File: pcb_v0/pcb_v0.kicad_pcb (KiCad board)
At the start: 2 copper layers, 1 part, among them U1 ATtiny2313-20P

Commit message: saved
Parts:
- added J1: Screw_Terminal_01x03, TerminalBlock_MetzConnect:TerminalBlock_MetzConnect_Type055_RT01503HDWU_1x03_P5.00mm_Horizontal, F.Cu at (113.1, 67.3)
- added NIX1: ~, nixie:in-8, F.Cu at (151.1, 81.3)
- added NIX2: ~, nixie:in-8, F.Cu at (171.1, 81.3)
- added NIX3: ~, nixie:in-8, F.Cu at (201.1, 81.3)
- added NIX4: ~, nixie:in-8, F.Cu at (221.1, 81.3)
- added NIX5: ~, nixie:in-8, F.Cu at (251.1, 81.3)
- added NIX6: ~, nixie:in-8, F.Cu at (271.1, 81.3)
- added U10: 74141, Package_DIP:DIP-16_W7.62mm_LongPads, F.Cu at (256.5, 71.1)
- added U2: 74141, Package_DIP:DIP-16_W7.62mm_LongPads, F.Cu at (148.6, 71.1)
- added U3: 74141, Package_DIP:DIP-16_W7.62mm_LongPads, F.Cu at (170.2, 71.1)
- added U4: 74141, Package_DIP:DIP-16_W7.62mm_LongPads, F.Cu at (191.8, 71.1)
- added U5: 74LS377, Package_DIP:DIP-20_W7.62mm_LongPads, F.Cu at (199.4, 100.3)
- added U6: 74141, Package_DIP:DIP-16_W7.62mm_LongPads, F.Cu at (213.3, 71.1)
- added U7: 74141, Package_DIP:DIP-16_W7.62mm_LongPads, F.Cu at (234.9, 71.1)
- added U8: 74LS377, Package_DIP:DIP-20_W7.62mm_LongPads, F.Cu at (149.9, 101.6)
- added U9: 74LS377, Package_DIP:DIP-20_W7.62mm_LongPads, F.Cu at (250.2, 100.3)
- moved U1 63.5 mm to (109.2, 17.8)
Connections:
- U1 pad 10: unconnected-(U1-GND-Pad10) -> GND
- U1 pad 12: unconnected-(U1-PB0-Pad12) -> Net-(U1-PB0)
- U1 pad 13: unconnected-(U1-PB1-Pad13) -> Net-(U1-PB1)
- U1 pad 14: unconnected-(U1-PB2-Pad14) -> Net-(U1-PB2)
- U1 pad 15: unconnected-(U1-PB3-Pad15) -> Net-(U1-PB3)
- U1 pad 16: unconnected-(U1-PB4-Pad16) -> Net-(U1-PB4)
- U1 pad 17: unconnected-(U1-PB5-Pad17) -> Net-(U1-PB5)
- U1 pad 18: unconnected-(U1-PB6-Pad18) -> Net-(U1-PB6)
- U1 pad 19: unconnected-(U1-PB7-Pad19) -> Net-(U1-PB7)
- U1 pad 20: unconnected-(U1-VCC-Pad20) -> +5V
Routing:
- net unconnected-(U1-VCC-Pad20): track 59.6 -> 0.00 mm

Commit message: saved
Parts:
- U1: footprint Package_DIP:DIP-20_W7.62mm -> Package_DIP:DIP-20_W7.62mm_LongPads
- moved J1 103.1 mm to (216.0, 61.0)
- moved U2 95.3 mm to (55.8, 49.5)
- moved NIX1 95.3 mm to (58.3, 59.7)
- moved NIX2 95.3 mm to (78.3, 59.7)
- moved NIX3 95.3 mm to (108.3, 59.7)
- moved NIX4 95.3 mm to (128.3, 59.7)
- moved NIX5 95.3 mm to (158.3, 59.7)
- moved NIX6 95.3 mm to (178.3, 59.7)
- moved U3 95.3 mm to (77.4, 49.5)
- moved U4 95.3 mm to (99.0, 49.5)
- moved U6 95.3 mm to (120.6, 49.5)
- moved U7 95.3 mm to (142.1, 49.5)
- moved U9 95.3 mm to (157.4, 78.8)
- moved U10 95.3 mm to (163.7, 49.5)
- moved U8 94.3 mm to (58.3, 78.8)
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
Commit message: saved
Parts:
- U1, U5, U8, U9: footprint Package_DIP:DIP-20_W7.62mm_LongPads -> Package_DIP:DIP-20_W7.62mm
- U10, U2, U3, U4, U6, U7: footprint Package_DIP:DIP-16_W7.62mm_LongPads -> Package_DIP:DIP-16_W7.62mm
- moved J1 165.8 mm to (50.3, 66.0), turned to 90 degrees
- moved U7 14.7 mm to (152.9, 59.6), turned to 160 degrees
- moved U3 13.1 mm to (88.9, 43.3), turned to 20 degrees
- moved U8 10.7 mm to (68.9, 76.9), turned to 80 degrees
- moved U6 10.6 mm to (130.2, 53.8), turned to 120 degrees
- moved U2 10.2 mm to (65.3, 53.2), turned to 103 degrees
- moved NIX1 6.50 mm to (64.4, 62.1)
- moved NIX2 6.50 mm to (84.4, 62.1)
- moved NIX3 6.50 mm to (114.4, 62.1)
- moved NIX4 6.50 mm to (134.4, 62.1)
- moved NIX5 6.50 mm to (164.4, 62.1)
- moved NIX6 6.50 mm to (184.4, 62.1)
- moved U4 6.12 mm to (103.2, 45.1), turned to 60 degrees
- moved U1 5.24 mm to (98.6, 81.2)
- moved U5 5.02 mm to (127.5, 81.2)
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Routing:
- net Net-(U1-PB3): track 0.00 -> 82.1 mm
- net Net-(U1-PB2): track 0.00 -> 71.8 mm
- net Net-(U1-PB1): track 0.00 -> 60.0 mm
- net Net-(U1-PB0): track 0.00 -> 53.8 mm
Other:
- board outline added: 170 x 50 mm

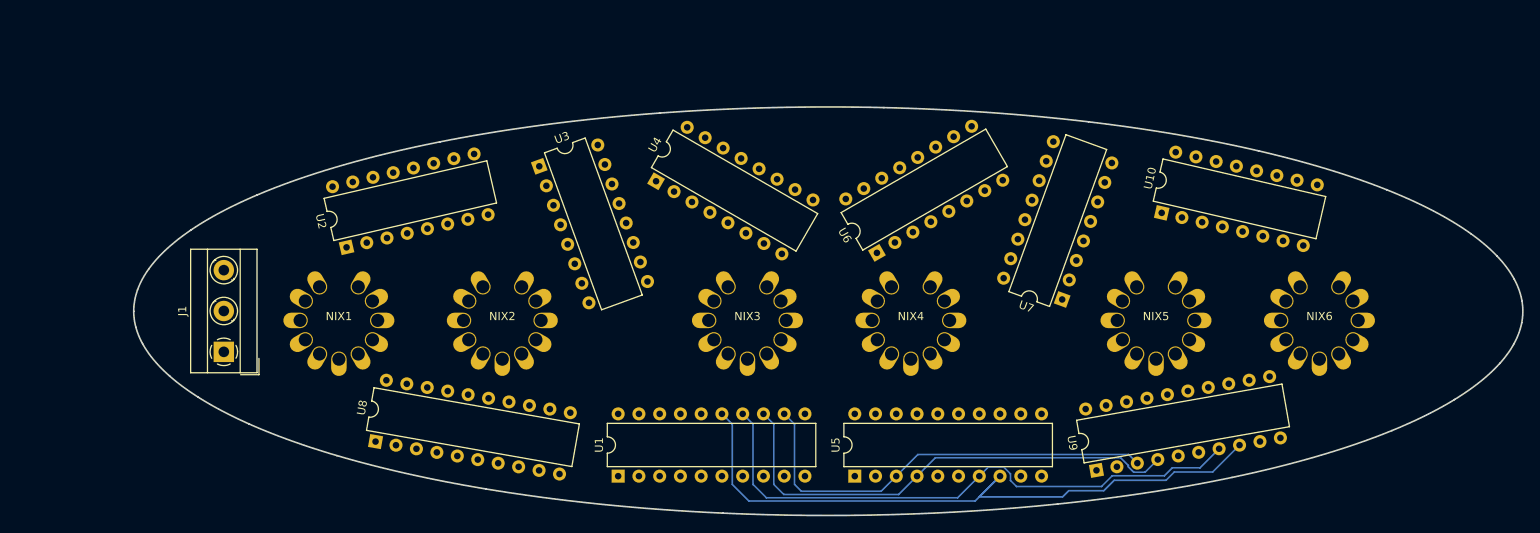
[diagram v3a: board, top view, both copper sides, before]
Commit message: ATtiny and flip flops routed
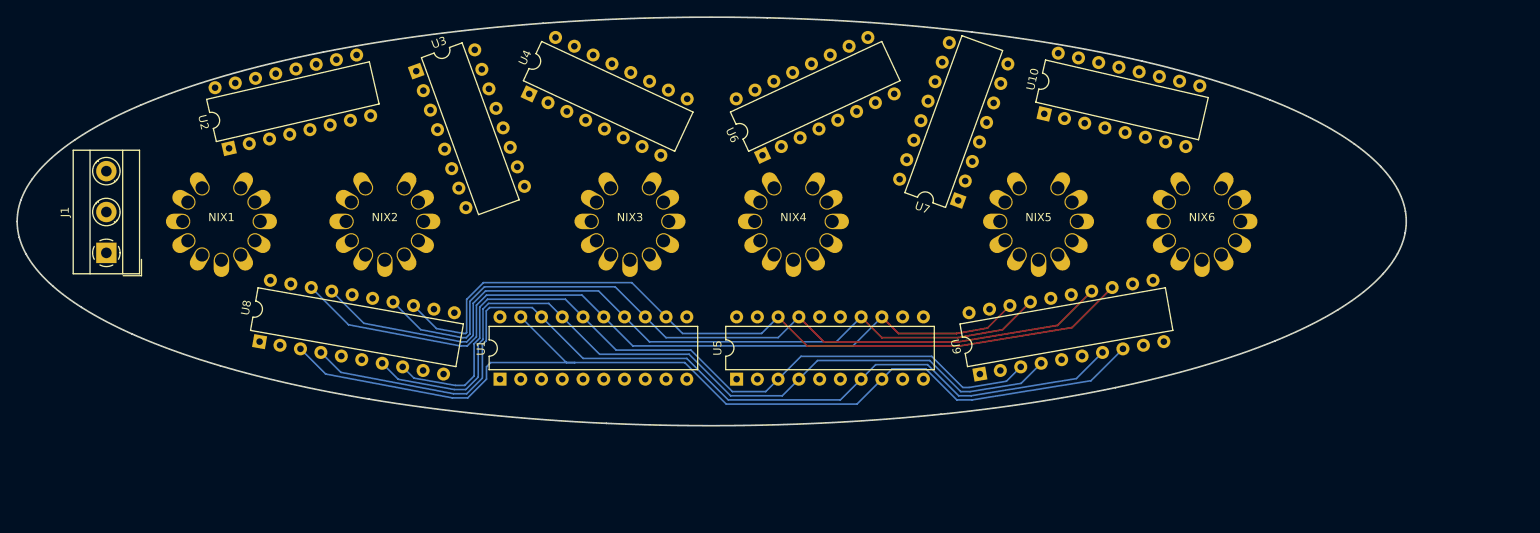
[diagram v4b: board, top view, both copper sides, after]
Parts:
- moved U3 19.0 mm to (73.8, 31.6)
- moved U4 18.8 mm to (87.7, 34.4), turned to 65 degrees
- moved U10 18.8 mm to (150.7, 36.8)
- moved J1 18.8 mm to (35.9, 53.8)
- moved NIX1 18.8 mm to (50.0, 50.0)
- moved NIX2 18.8 mm to (70.0, 50.0)
- moved NIX3 18.8 mm to (100.0, 50.0)
- moved NIX4 18.8 mm to (120.0, 50.0)
- moved NIX5 18.8 mm to (150.0, 50.0)
- moved NIX6 18.8 mm to (170.0, 50.0)
- moved U2 18.8 mm to (50.9, 41.1)
- moved U8 18.7 mm to (54.7, 64.7)
- moved U1 18.7 mm to (84.1, 69.3)
- moved U5 18.7 mm to (113.0, 69.3)
- moved U9 18.5 mm to (142.8, 68.7)
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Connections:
- U5 pad 13: Net-(U1-PB4) -> Net-(U1-PB3)
- U5 pad 14: Net-(U1-PB5) -> Net-(U1-PB2)
- U5 pad 17: Net-(U1-PB6) -> Net-(U1-PB1)
- U5 pad 18: Net-(U1-PB7) -> Net-(U1-PB0)
- U5 pad 3: Net-(U1-PB0) -> Net-(U1-PB4)
- U5 pad 4: Net-(U1-PB1) -> Net-(U1-PB5)
- U5 pad 7: Net-(U1-PB2) -> Net-(U1-PB6)
- U5 pad 8: Net-(U1-PB3) -> Net-(U1-PB7)
- U8 pad 13: Net-(U1-PB4) -> Net-(U1-PB0)
- U8 pad 14: Net-(U1-PB5) -> Net-(U1-PB1)
- U8 pad 17: Net-(U1-PB6) -> Net-(U1-PB2)
- U8 pad 18: Net-(U1-PB7) -> Net-(U1-PB3)
- U8 pad 3: Net-(U1-PB0) -> Net-(U1-PB7)
- U8 pad 4: Net-(U1-PB1) -> Net-(U1-PB6)
- U8 pad 7: Net-(U1-PB2) -> Net-(U1-PB5)
- U8 pad 8: Net-(U1-PB3) -> Net-(U1-PB4)
- U9 pad 13: Net-(U1-PB4) -> Net-(U1-PB0)
- U9 pad 14: Net-(U1-PB5) -> Net-(U1-PB1)
- U9 pad 17: Net-(U1-PB6) -> Net-(U1-PB2)
- U9 pad 18: Net-(U1-PB7) -> Net-(U1-PB3)
- U9 pad 3: Net-(U1-PB0) -> Net-(U1-PB4)
- U9 pad 4: Net-(U1-PB1) -> Net-(U1-PB5)
- U9 pad 7: Net-(U1-PB2) -> Net-(U1-PB6)
- U9 pad 8: Net-(U1-PB3) -> Net-(U1-PB7)
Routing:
- net Net-(U1-PB7): track 0.00 -> 121.2 mm
- net Net-(U1-PB6): track 0.00 -> 115.4 mm
- net Net-(U1-PB5): track 0.00 -> 99.6 mm
- net Net-(U1-PB4): track 0.00 -> 94.0 mm
- net Net-(U1-PB0): track 53.8 -> 98.8 mm
- net Net-(U1-PB1): track 60.0 -> 98.7 mm
- net Net-(U1-PB2): track 71.8 -> 98.6 mm
- net Net-(U1-PB3): track 82.1 -> 98.6 mm

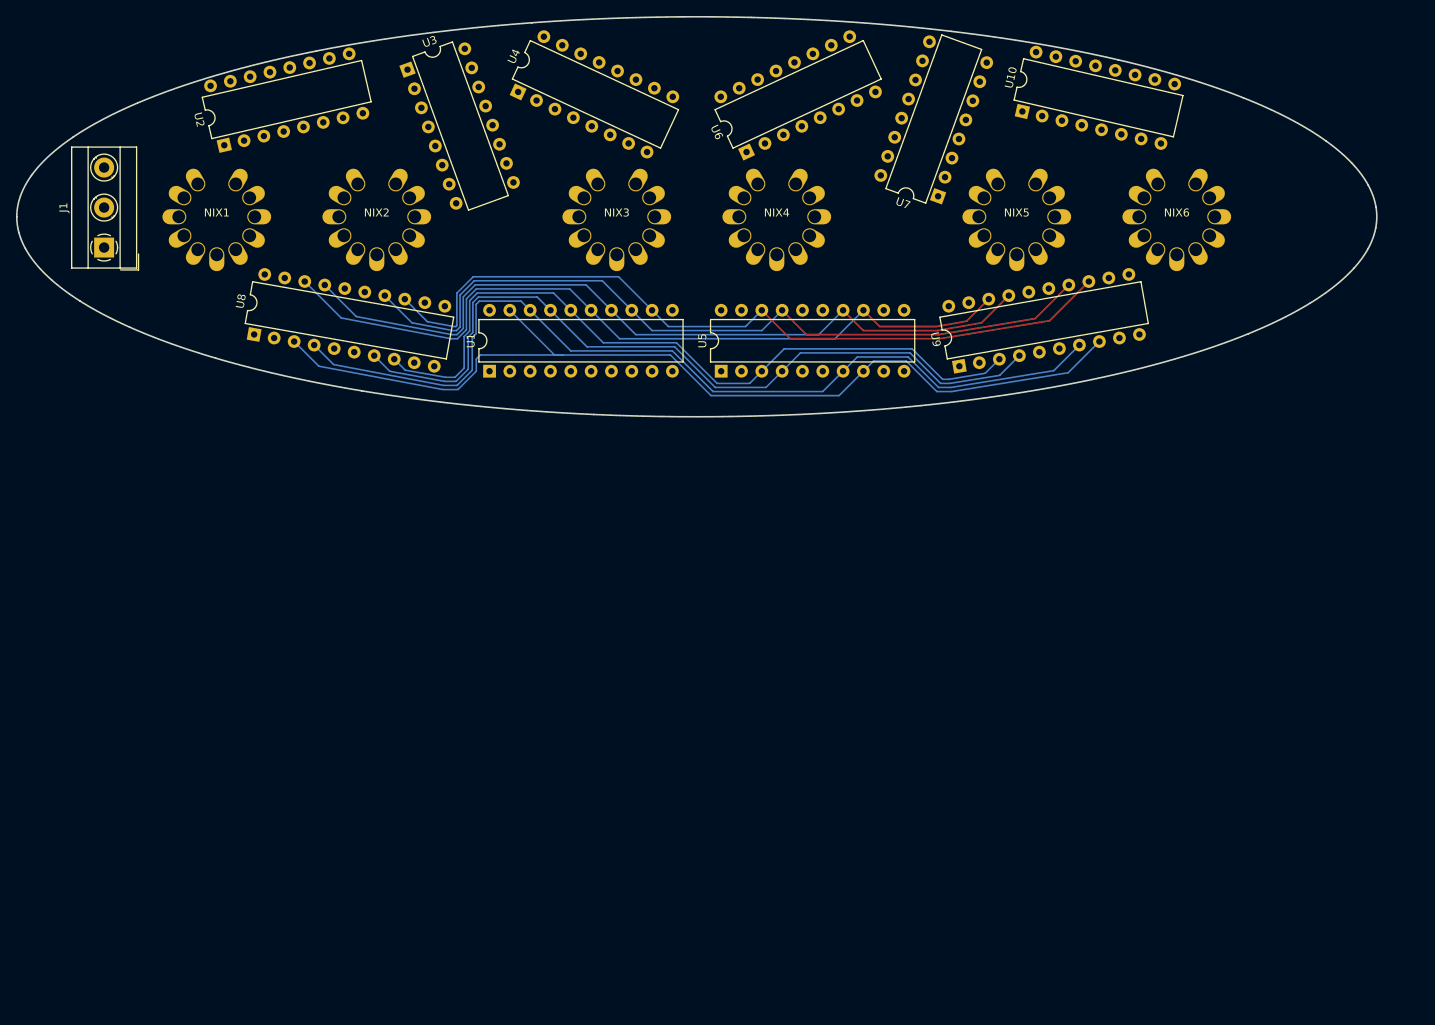
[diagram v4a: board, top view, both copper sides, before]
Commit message: new outline, now nothing fits
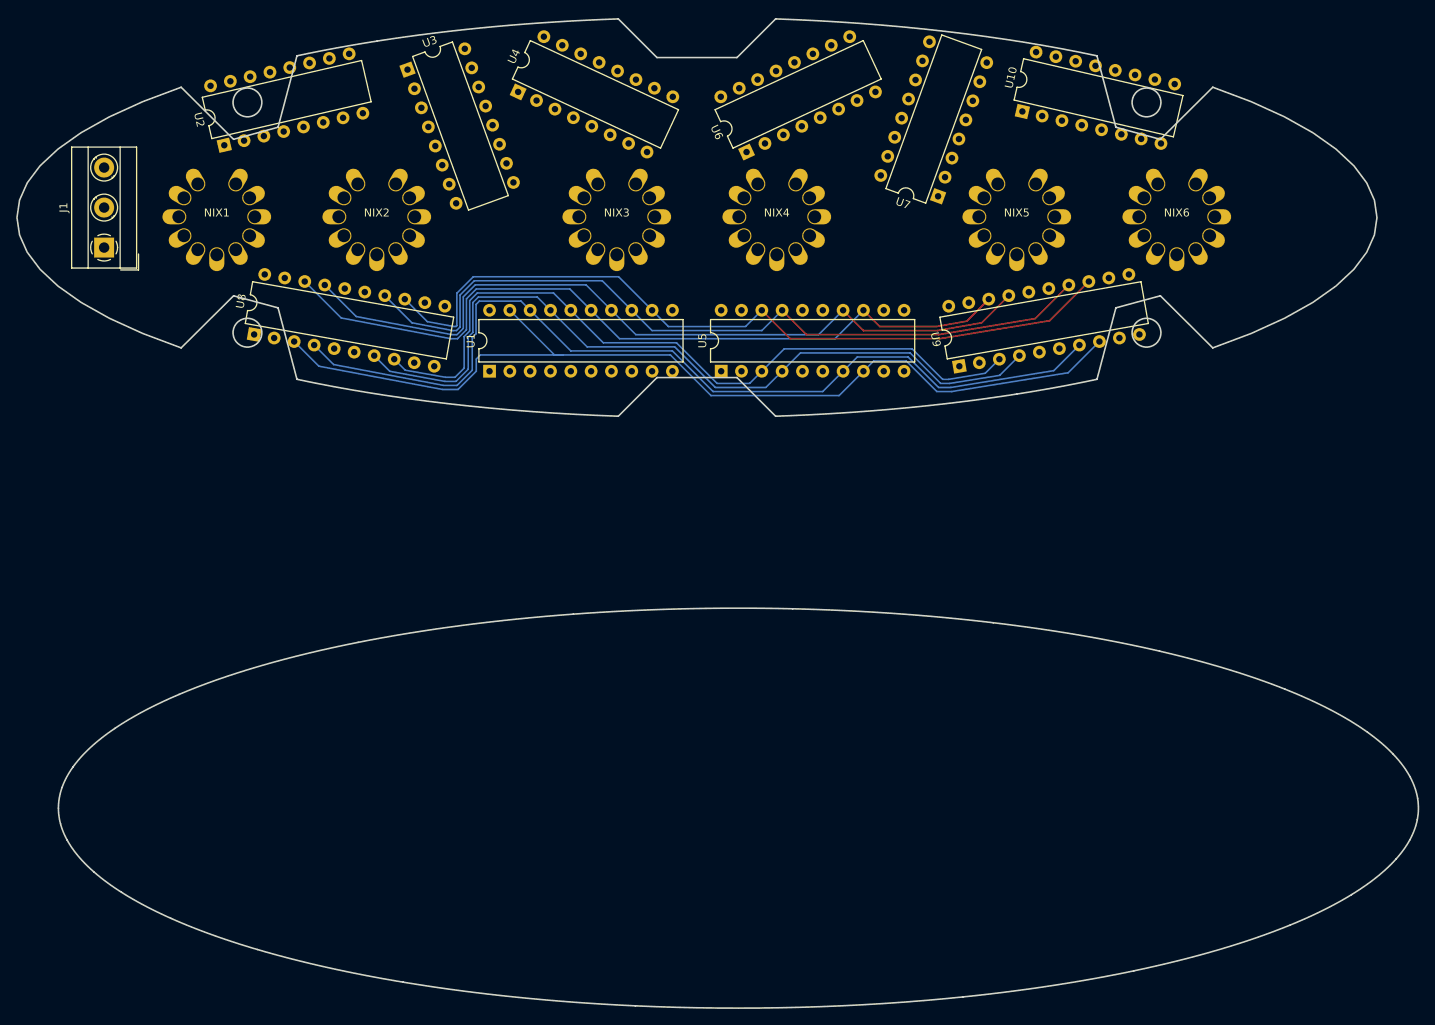
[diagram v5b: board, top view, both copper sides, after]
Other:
- board size 170 x 50 mm -> 175.2 x 123.7 mm

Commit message: save
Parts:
- added NE1: Lamp_Neon, Connector_PinSocket_1.27mm:PinSocket_1x02_P1.27mm_Vertical, F.Cu at (84.4, 49.5)
- added NE2: Lamp_Neon, Connector_PinSocket_1.27mm:PinSocket_1x02_P1.27mm_Vertical, F.Cu at (135.6, 49.5)
- added Q1: Q_NMOS_GDS, Package_TO_SOT_SMD:SOT-223-3_TabPin2, F.Cu at (156.3, 36.7)
- added R1: R_US, Resistor_THT:R_Axial_DIN0204_L3.6mm_D1.6mm_P2.54mm_Vertical, F.Cu at (58.6, 45.6)
- added R2: R_US, Resistor_THT:R_Axial_DIN0204_L3.6mm_D1.6mm_P2.54mm_Vertical, F.Cu at (78.2, 45.6)
- added R3: R_US, Resistor_THT:R_Axial_DIN0204_L3.6mm_D1.6mm_P2.54mm_Vertical, F.Cu at (108.1, 44.9)
- added R4: R_US, Resistor_THT:R_Axial_DIN0204_L3.6mm_D1.6mm_P2.54mm_Vertical, F.Cu at (129.1, 46.2)
- added R5: R_US, Resistor_THT:R_Axial_DIN0204_L3.6mm_D1.6mm_P2.54mm_Vertical, F.Cu at (158.3, 45.6)
- added R6: R_US, Resistor_THT:R_Axial_DIN0204_L3.6mm_D1.6mm_P2.54mm_Vertical, F.Cu at (175.4, 42.2)
- added R7: R_US, Resistor_THT:R_Axial_DIN0204_L3.6mm_D1.6mm_P2.54mm_Vertical, F.Cu at (86.5, 53.8)
- added R8: R_US, Resistor_THT:R_Axial_DIN0204_L3.6mm_D1.6mm_P2.54mm_Vertical, F.Cu at (137.7, 53.8)
- J1: footprint TerminalBlock_MetzConnect:TerminalBlock_MetzConnect_Type055_RT01503HDWU_1x03_P5.00mm_Horizontal -> Connector_PinHeader_2.54mm:PinHeader_1x03_P2.54mm_Vertical
- moved J1 113.9 mm to (148.1, 34.1), turned to 0 degrees
- moved U10 28.2 mm to (178.6, 41.1), turned to 0 degrees
- moved U7 17.4 mm to (124.0, 41.1), turned to 90 degrees
- moved U2 17.1 mm to (33.8, 41.1), turned to 0 degrees
- moved U3 15.9 mm to (61.1, 41.1), turned to 90 degrees
- moved U6 13.2 mm to (103.0, 41.1), turned to 90 degrees
- moved U4 8.75 mm to (82.1, 41.1), turned to 90 degrees
- moved U9 5.95 mm to (137.5, 66.0), turned to 90 degrees
- moved U8 5.04 mm to (59.6, 66.0), turned to 90 degrees
- moved U1 2.51 mm to (85.6, 67.3)
- moved U5 2.51 mm to (111.6, 67.3)
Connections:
- U8 pad 13: Net-(U1-PB0) -> Net-(U1-PB7)
- U8 pad 14: Net-(U1-PB1) -> Net-(U1-PB6)
- U8 pad 17: Net-(U1-PB2) -> Net-(U1-PB5)
- U8 pad 18: Net-(U1-PB3) -> Net-(U1-PB4)
- U8 pad 3: Net-(U1-PB7) -> Net-(U1-PB3)
- U8 pad 4: Net-(U1-PB6) -> Net-(U1-PB2)
- U8 pad 7: Net-(U1-PB5) -> Net-(U1-PB1)
- U8 pad 8: Net-(U1-PB4) -> Net-(U1-PB0)
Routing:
- net Net-(U1-PB7): track 121.2 -> 12.4 mm
- net Net-(U1-PB6): track 115.4 -> 17.9 mm
- net Net-(U1-PB5): track 99.6 -> 28.5 mm
- net Net-(U1-PB0): track 98.8 -> 31.2 mm
- net Net-(U1-PB1): track 98.7 -> 31.2 mm
- net Net-(U1-PB2): track 98.6 -> 36.2 mm
- net Net-(U1-PB3): track 98.6 -> 36.2 mm
- net Net-(U1-PB4): track 94.0 -> 34.0 mm
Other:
- board size 175.2 x 123.7 mm -> 170 x 50 mm

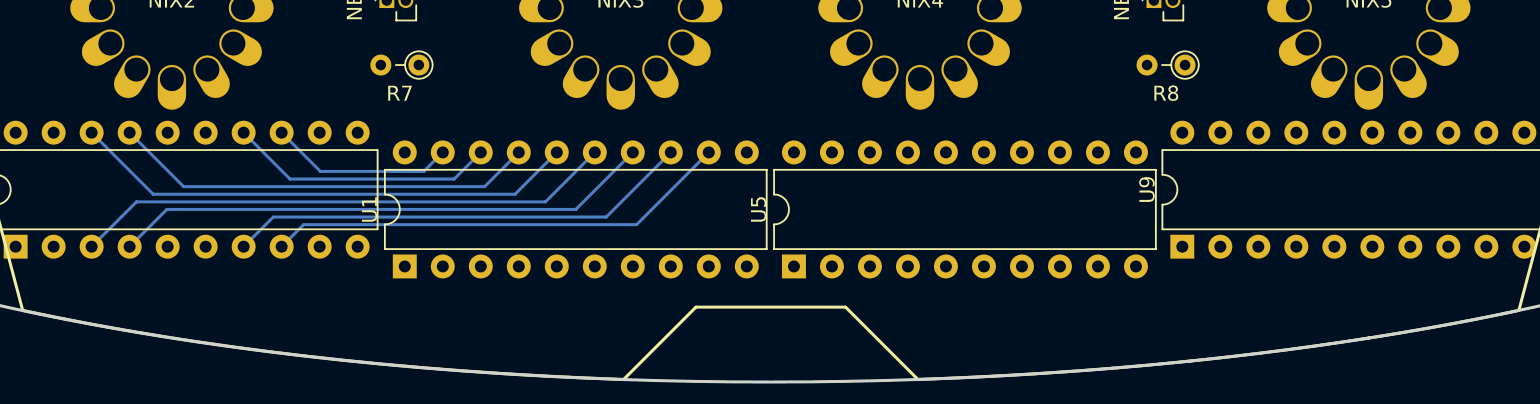
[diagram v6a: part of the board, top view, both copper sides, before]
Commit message: registers wired correctly this time
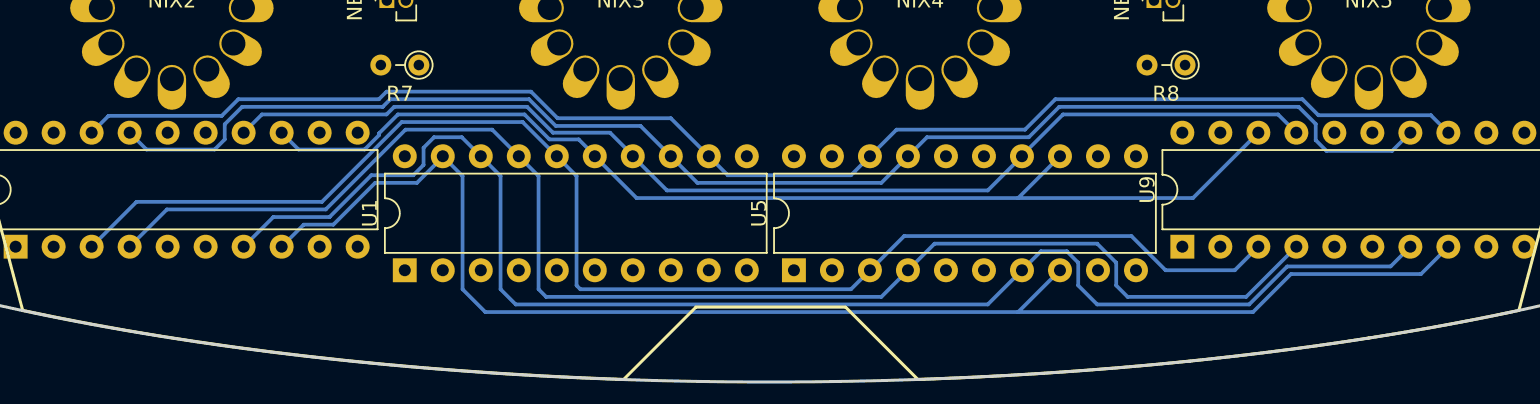
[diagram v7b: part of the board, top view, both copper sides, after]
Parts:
- moved U1 0.25 mm to (85.6, 67.5)
- moved U5 0.25 mm to (111.6, 67.5)
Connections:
- U8 pad 13: Net-(U1-PB7) -> Net-(U1-PB3)
- U8 pad 14: Net-(U1-PB6) -> Net-(U1-PB2)
- U8 pad 17: Net-(U1-PB5) -> Net-(U1-PB1)
- U8 pad 18: Net-(U1-PB4) -> Net-(U1-PB0)
- U8 pad 3: Net-(U1-PB3) -> Net-(U1-PB4)
- U8 pad 4: Net-(U1-PB2) -> Net-(U1-PB5)
- U8 pad 7: Net-(U1-PB1) -> Net-(U1-PB6)
- U8 pad 8: Net-(U1-PB0) -> Net-(U1-PB7)
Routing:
- net Net-(U1-PB7): track 12.4 -> 95.0 mm
- net Net-(U1-PB6): track 17.9 -> 96.2 mm
- net Net-(U1-PB5): track 28.5 -> 95.5 mm
- net Net-(U1-PB0): track 31.2 -> 97.2 mm
- net Net-(U1-PB1): track 31.2 -> 94.8 mm
- net Net-(U1-PB4): track 34.0 -> 93.4 mm
- net Net-(U1-PB2): track 36.2 -> 76.1 mm
- net Net-(U1-PB3): track 36.2 -> 74.9 mm

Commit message: save
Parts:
- moved R6 1.54 mm to (175.5, 43.7)
- moved R1 1.23 mm to (57.4, 46.0)
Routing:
- net Net-(U2-D): track 0.00 -> 62.7 mm
- net Net-(NIX1-cathode8): track 0.00 -> 45.5 mm
- net Net-(U2-C): track 0.00 -> 45.1 mm
- net Net-(U2-B): track 0.00 -> 44.5 mm
- net Net-(U2-A): track 0.00 -> 43.0 mm
- net Net-(NIX6-cathode4): track 0.00 -> 39.2 mm
- net Net-(NIX6-cathode5): track 0.00 -> 37.0 mm
- net Net-(NIX6-cathode3): track 0.00 -> 32.0 mm
- net Net-(NIX1-cathode9): track 0.00 -> 31.0 mm
- net Net-(NIX6-cathode2): track 0.00 -> 30.0 mm
- net Net-(NIX1-cathode5): track 0.00 -> 29.4 mm
- net Net-(NIX6-cathode1): track 0.00 -> 26.7 mm
- net Net-(NIX6-cathode7): track 0.00 -> 20.4 mm
- net Net-(NIX1-cathode2): track 0.00 -> 20.1 mm
- net Net-(NIX6-cathode6): track 0.00 -> 19.8 mm
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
